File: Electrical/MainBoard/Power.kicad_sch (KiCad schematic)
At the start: 17 parts, among them J13 USB_B_Micro, J14 Battery1, J4 5V Supply, J5 3.3V Supply, SW1 5V Bypass, SW2 All Power Switch, U1 AP2114HA-3.3TRG1

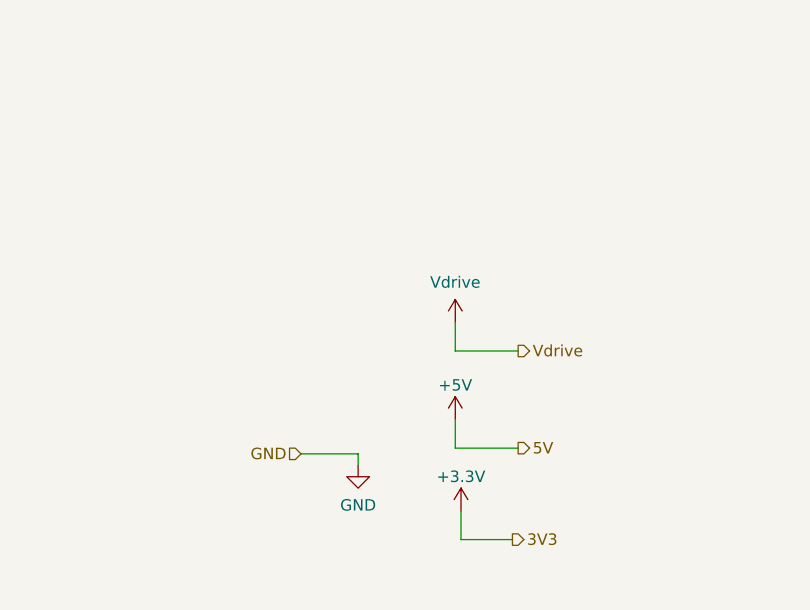
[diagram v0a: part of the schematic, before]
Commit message: Add more schematics and begin floorplanning
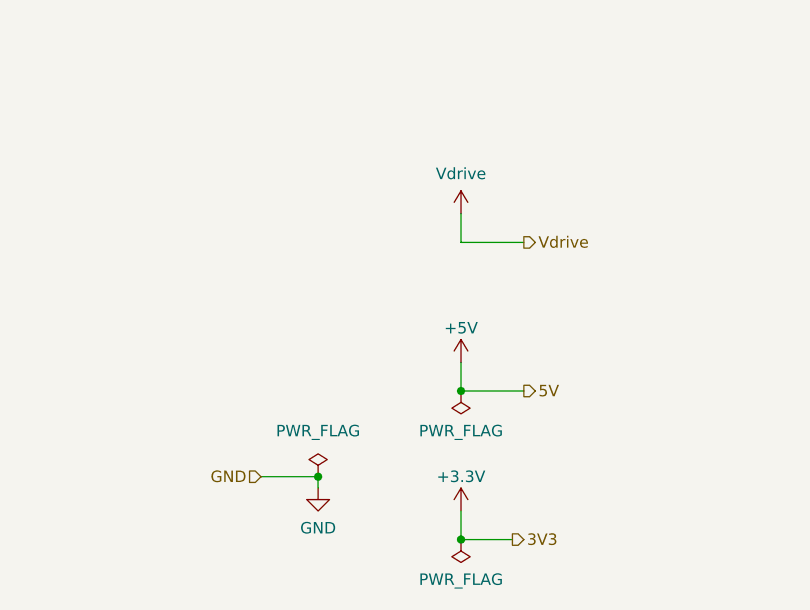
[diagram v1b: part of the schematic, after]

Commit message: Begin layout of pcb
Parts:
- renumbered J5 to J2, J4 to J3

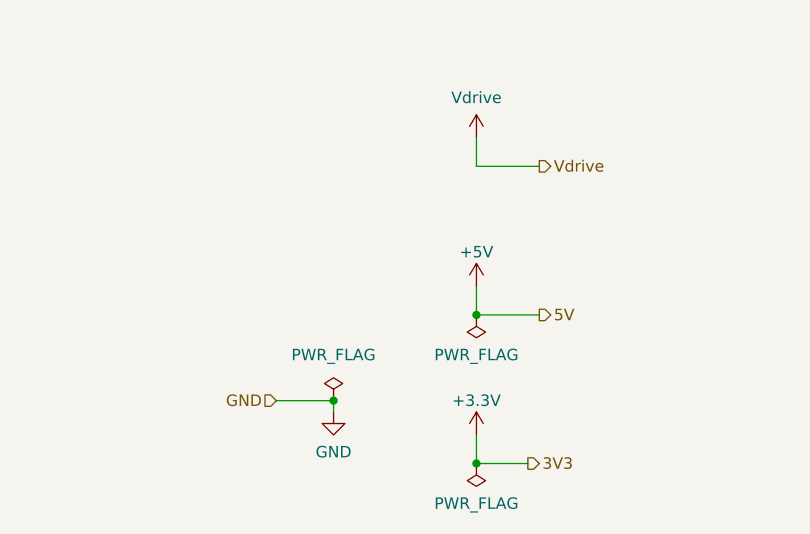
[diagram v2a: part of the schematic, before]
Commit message: First Pass at the routing
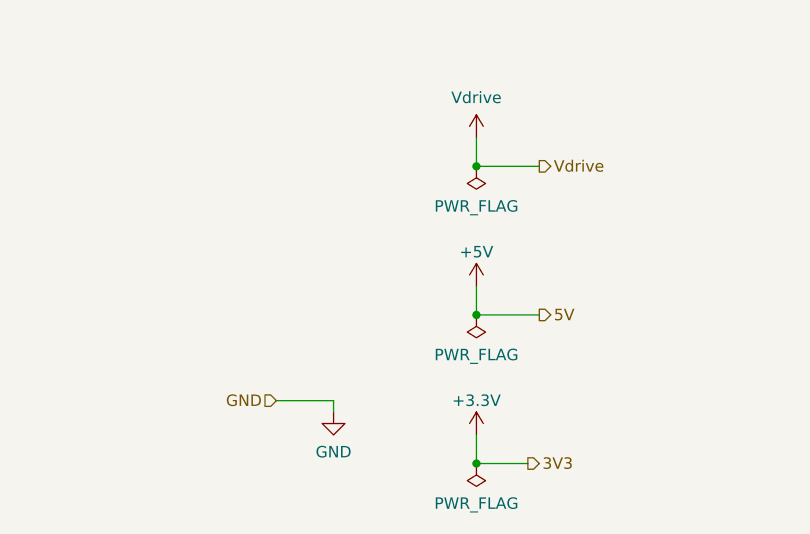
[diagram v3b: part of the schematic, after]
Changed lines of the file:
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@@
     (comment 4 "Matthew Sato")
   )
+  (junction (at 285.115 227.965) (diameter 0) (color 0 0 0 0)
+  )
   (junction (at 209.55 135.89) (diameter 0) (color 0 0 0 0)
   )
@@
   )
   (junction (at 132.08 145.415) (diameter 0) (color 0 0 0 0)
-  )
-  (junction (at 269.24 254) (diameter 0) (color 0 0 0 0)
   )
   (junction (at 168.275 56.515) (diameter 0) (color 0 0 0 0)
@@
         (path "/bd24c4db-4e36-4117-bd4f-5228ef241da9/8ba935aa-d6da-451b-8954-3c3ef7086bfd"
           (reference "C11") (unit 1)
-        )
-      )
-    )
-  )
-  (symbol (lib_id "power:PWR_FLAG") (at 269.24 254 0) (unit 1)
-    (in_bom yes) (on_board yes) (dnp no) (fields_autoplaced)
-    (property "Reference" "#FLG01" (at 269.24 252.095 0)
-      (effects (font (size 1.27 1.27)) hide)
-    )
-    (property "Value" "PWR_FLAG" (at 269.24 248.92 0)
-      (effects (font (size 1.27 1.27)))
-    )
-    (property "Footprint" "" (at 269.24 254 0)
-      (effects (font (size 1.27 1.27)) hide)
-    )
-    (property "Datasheet" "~" (at 269.24 254 0)
-      (effects (font (size 1.27 1.27)) hide)
-    )
-    (pin "1")
-    (instances
-      (project "MainBoard"
-        (path "/bd24c4db-4e36-4117-bd4f-5228ef241da9/8ba935aa-d6da-451b-8954-3c3ef7086bfd"
-          (reference "#FLG01") (unit 1)
         )
       )
@@
         )
       )
+    )
+  )
+  (symbol (lib_id "power:PWR_FLAG") (at 285.115 227.965 180) (unit 1)
+    (in_bom yes) (on_board yes) (dnp no) (fields_autoplaced)
+    (property "Reference" "#FLG01" (at 285.115 229.87 0)
+      (effects (font (size 1.27 1.27)) hide)
+    )
+    (property "Value" "PWR_FLAG" (at 285.115 232.41 0)
+      (effects (font (size 1.27 1.27)))
+    )
+    (property "Footprint" "" (at 285.115 227.965 0)
+      (effects (font (size 1.27 1.27)) hide)
+    )
+    (property "Datasheet" "~" (at 285.115 227.965 0)
+      (effects (font (size 1.27 1.27)) hide)
+    )
+    (pin "1")
+    (instances
+      (project "MainBoard"
+        (path "/bd24c4db-4e36-4117-bd4f-5228ef241da9/8ba935aa-d6da-451b-8954-3c3ef7086bfd"
+          (reference "#FLG01") (unit 1)
+        )
+      )

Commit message: Add some finishing touches and create preliminary boms
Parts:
- D1: value ON -> LED
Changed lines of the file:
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@@
       (effects (font (size 1.27 1.27)) (justify right))
     )
-    (property "Value" "ON" (at 292.735 141.605 0)
+    (property "Value" "LED" (at 292.735 141.605 0)
       (effects (font (size 1.27 1.27)) (justify right))
     )

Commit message: Some finishing touches to the board
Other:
- note added: "Molex + Switch Female, DigiKey P/N: WM2124-ND Crimp, DigiKey P/N: WM20948CT-ND"
- note removed: "Molex + Switch"
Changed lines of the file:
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@@
     (effects (font (size 1.27 1.27)) (justify left bottom))
   )
-  (text "Molex + Switch" (at 258.445 55.245 0)
+  (text "Molex + Switch\n\nFemale, DigiKey P/N: WM2124-ND\nCrimp,  DigiKey P/N: WM20948CT-ND"
+    (at 250.825 53.34 0)
     (effects (font (size 1.27 1.27)) (justify left bottom))
   )

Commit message: Update the main power switch
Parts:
- SW2: Mfr Bulgin -> E-Switch; Mfr P/N C1553PBNAW -> RA83231100; Supplier 1 P/N 708-3039-ND -> EG5682-ND
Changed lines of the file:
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@@
       (effects (font (size 1.27 1.27)) hide)
     )
-    (property "Datasheet" "https://www.bulgin.com/products/pub/media/bulgin/data/C1550,%20C1350.pdf" (at 265.43 65.405 0)
+    (property "Datasheet" "https://sten-eswitch-13110800-production.s3.amazonaws.com/system/asset/product_line/data_sheet/84/RA8.pdf" (at 265.43 65.405 0)
       (effects (font (size 1.27 1.27)) hide)
     )
-    (property "Description" "SWITCH ROCKER DPST ILLUM" (at 265.43 65.405 0)
+    (property "Description" "SWITCH ROCKER DPST 16A 125V" (at 265.43 65.405 0)
       (effects (font (size 1.27 1.27)) hide)
     )
-    (property "Mfr" "Bulgin" (at 265.43 65.405 0)
+    (property "Mfr" "E-Switch" (at 265.43 65.405 0)
       (effects (font (size 1.27 1.27)) hide)
     )
-    (property "Mfr P/N" "C1553PBNAW" (at 265.43 65.405 0)
+    (property "Mfr P/N" "RA83231100" (at 265.43 65.405 0)
       (effects (font (size 1.27 1.27)) hide)
     )
@@
       (effects (font (size 1.27 1.27)) hide)
     )
-    (property "Supplier 1 P/N" "708-3039-ND" (at 265.43 65.405 0)
+    (property "Supplier 1 P/N" "EG5682-ND" (at 265.43 65.405 0)
       (effects (font (size 1.27 1.27)) hide)
     )

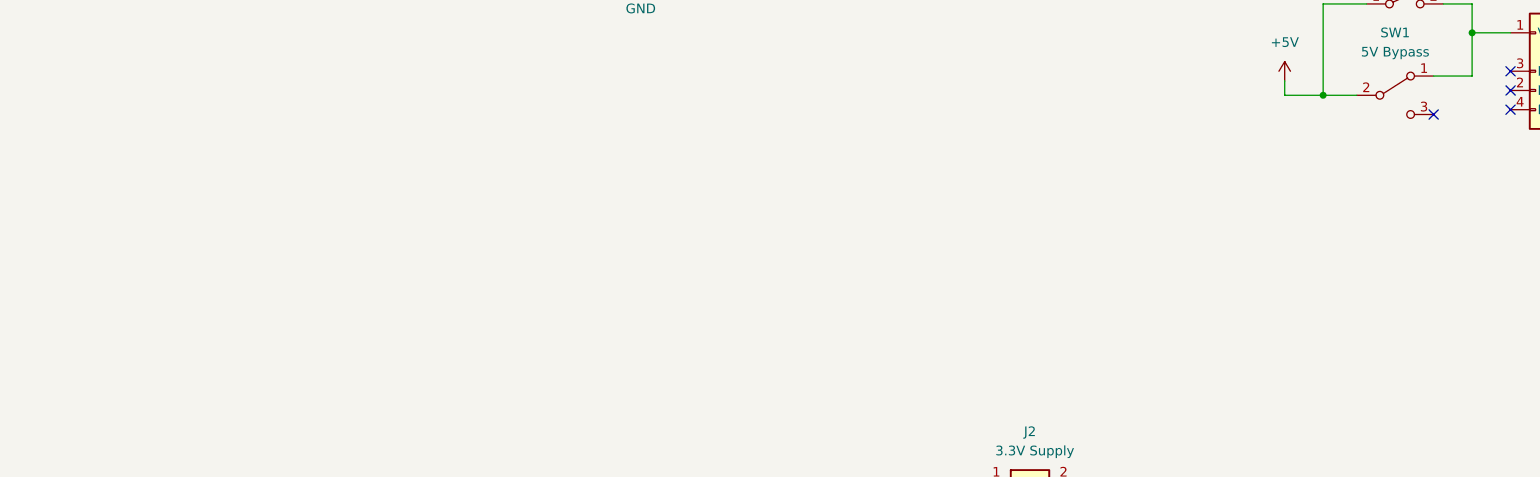
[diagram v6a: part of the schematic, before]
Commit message: Made a comment that we may need a small resistor to draw some current from battery to keep on
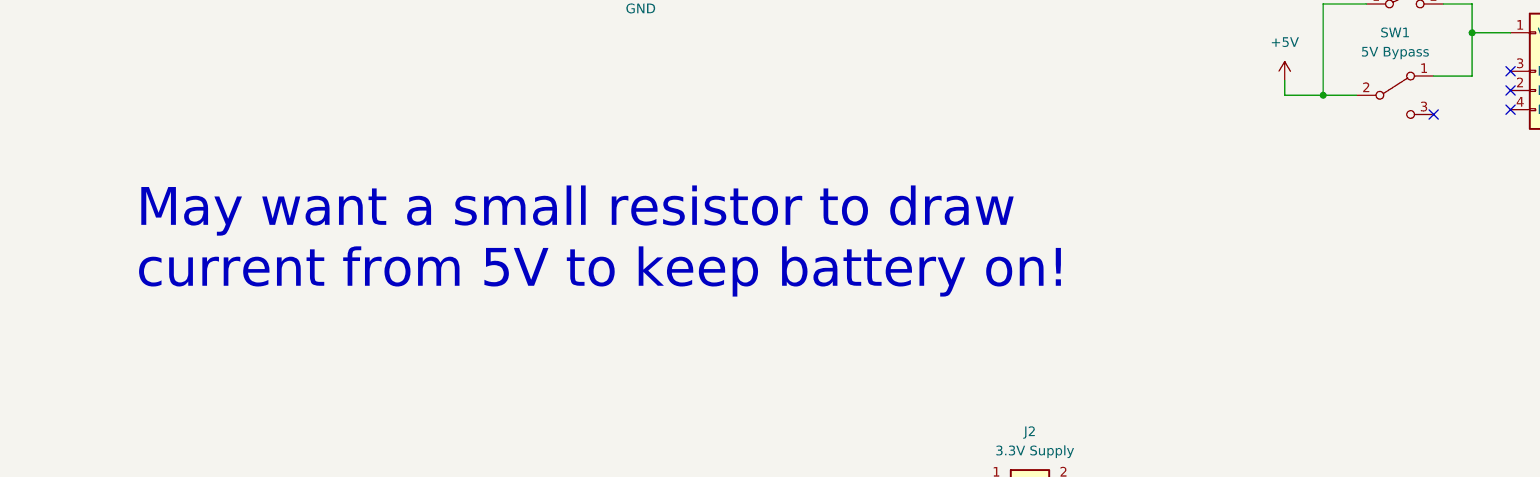
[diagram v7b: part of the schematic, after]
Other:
- note added: "May want a small resistor to draw current from 5V to keep battery on!"
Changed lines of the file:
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@@
     (effects (font (size 1.27 1.27)) (justify left bottom))
+  )
+  (text "May want a small resistor to draw\ncurrent from 5V to keep battery on!"
+    (at 97.79 106.045 0)
+    (effects (font (size 5 5)) (justify left bottom))
   )
   (text "Inputs:\n1) Motor Battery: 2x NiMH Battery, 7.2 V Each\n2) Battery For Jetson: 12 V\n3) Battery for MCU: 5 V"

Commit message: Made V0.2 revisions to Main Board
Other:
- note removed: "May want a small resistor to draw current from 5V to keep battery on!"
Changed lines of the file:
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@@
   (title_block
     (title "MCU Controller")
-    (rev "0.1")
+    (rev "0.2")
     (company "satomm@stanford.edu")
     (comment 1 "Department of Civil and Environmental Engineering")
@@
     (effects (font (size 1.27 1.27)) (justify left bottom))
   )
-  (text "May want a small resistor to draw\ncurrent from 5V to keep battery on!"
-    (at 97.79 106.045 0)
-    (effects (font (size 5 5)) (justify left bottom))
-  )
   (text "Inputs:\n1) Motor Battery: 2x NiMH Battery, 7.2 V Each\n2) Battery For Jetson: 12 V\n3) Battery for MCU: 5 V"
